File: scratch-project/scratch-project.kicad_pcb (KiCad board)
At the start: 4 copper layers, 98 x 98 mm, 13 parts, among them J1 Conn_01x10_Pin, J2 Conn_01x10_Pin, J3 Conn_02x10_Top_Bottom, J4 Conn_02x10_Top_Bottom, J5 Conn_02x10_Top_Bottom, J6 Conn_01x10_Pin

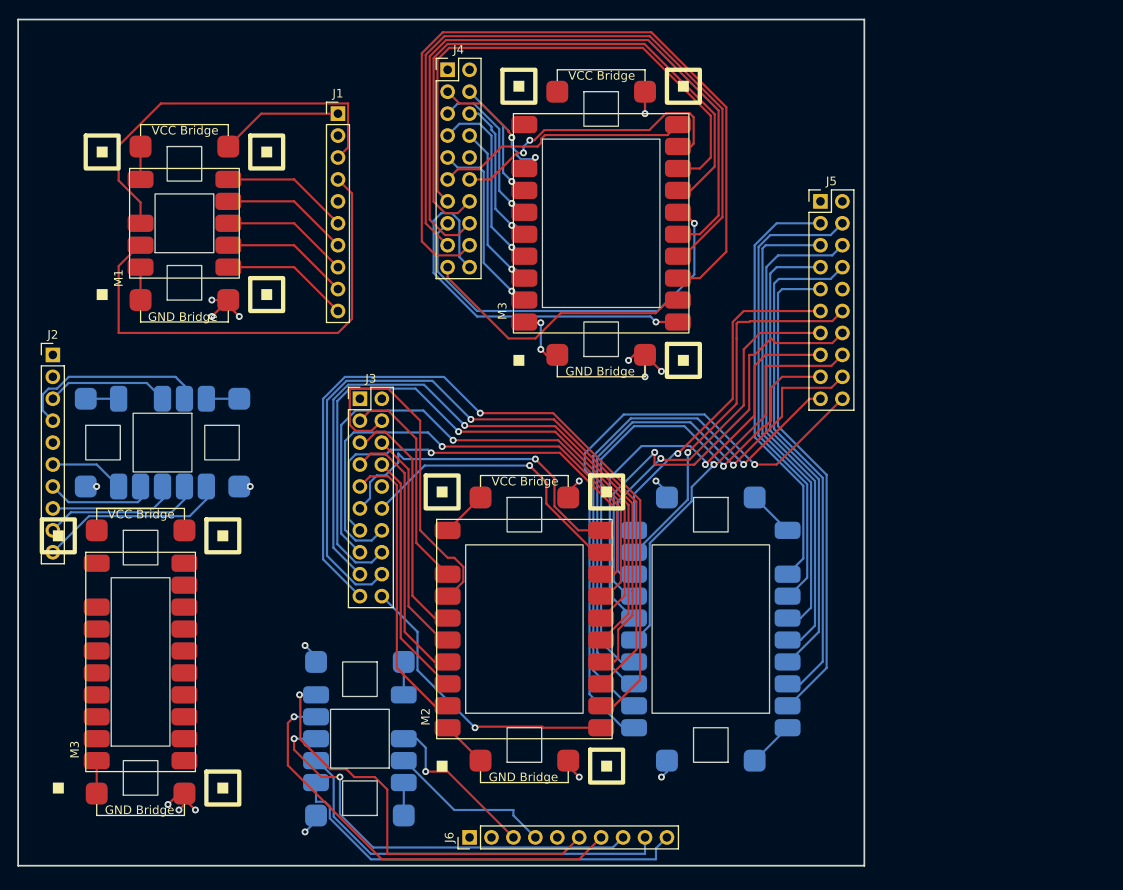
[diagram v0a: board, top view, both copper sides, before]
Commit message: fix pad sizes and schematic errors
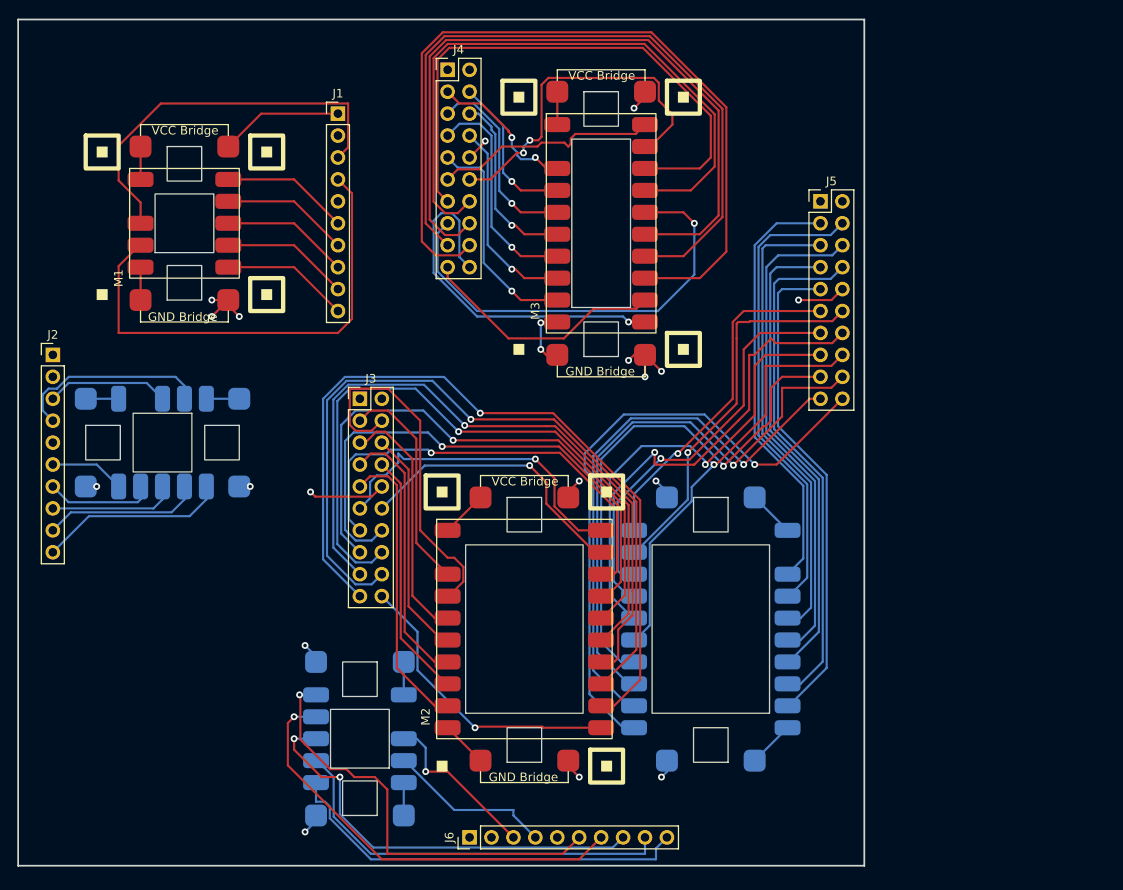
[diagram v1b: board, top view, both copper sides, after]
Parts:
- removed the M3 at (33.0, 91.4)
- M3: footprint MegaCastle:MegaCastle2x10Wide -> MegaCastle:MegaCastle2x10
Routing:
- net GND: track 24.0 -> 41.2 mm, vias 10 -> 13
- net unconnected-(M3-Board_GND-PadB2): track 7.03 -> 0.00 mm, vias 3 -> 0
- net Net-(J4-Pin_12): track 34.8 -> 40.7 mm
- net Net-(J4-Pin_16): track 80.2 -> 84.0 mm
- net Net-(J4-Pin_14): track 70.0 -> 73.8 mm
- net Net-(J4-Pin_19): track 32.6 -> 28.8 mm
- net Net-(M3-Module_VCC): track 0.00 -> 3.81 mm
- net Net-(J4-Pin_9): track 21.9 -> 25.7 mm
- net Net-(J4-Pin_8): track 19.4 -> 23.2 mm
- net Net-(J4-Pin_7): track 22.0 -> 25.8 mm
- net Net-(J4-Pin_6): track 17.4 -> 21.3 mm
- net Net-(J4-Pin_5): track 18.8 -> 22.6 mm
- net Net-(J4-Pin_20): track 46.3 -> 42.5 mm
- net Net-(J4-Pin_18): track 91.9 -> 95.8 mm
- net Net-(J4-Pin_17): track 81.4 -> 85.2 mm
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
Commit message: fix 2x10 wide footprint. add modules to scratch board
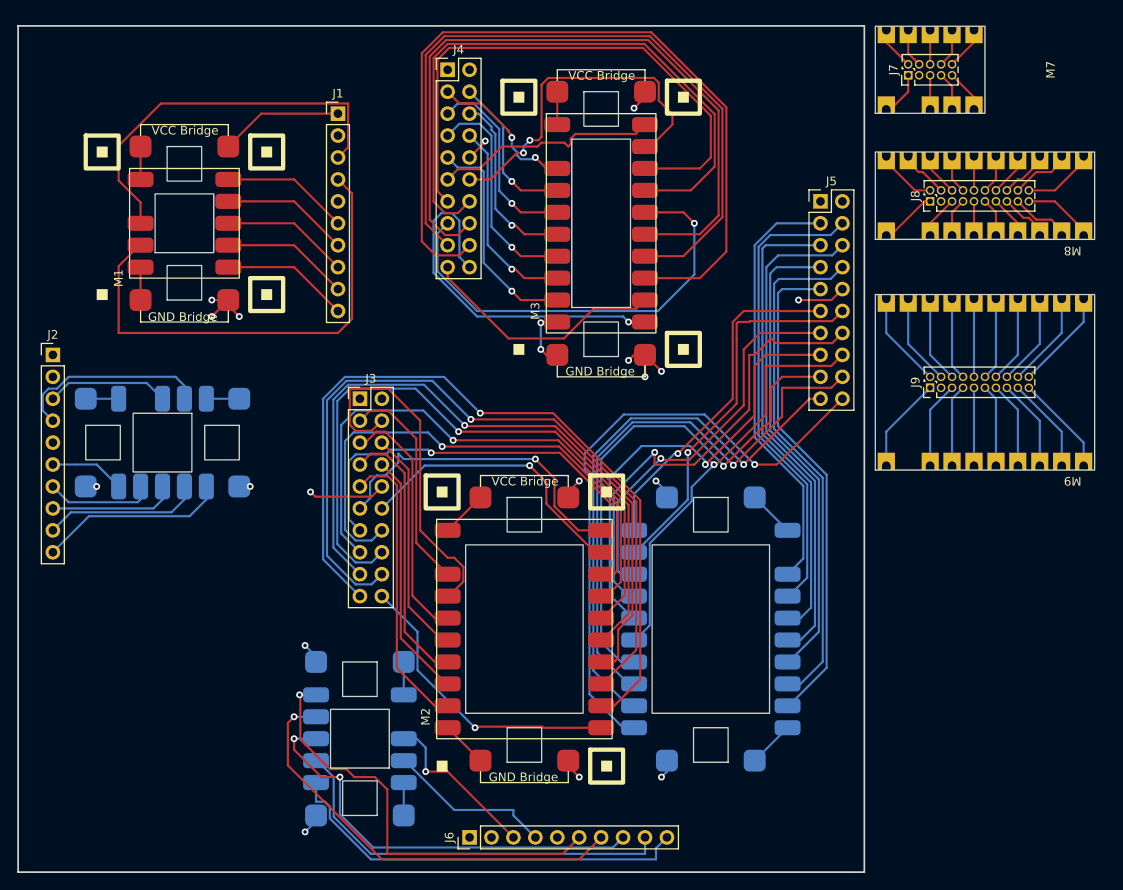
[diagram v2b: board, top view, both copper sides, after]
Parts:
- added J7: Conn_02x05_Top_Bottom, Connector_PinHeader_1.27mm:PinHeader_2x05_P1.27mm_Vertical, F.Cu at (121.9, 23.5)
- added J8: Conn_02x10_Top_Bottom, Connector_PinHeader_1.27mm:PinHeader_2x10_P1.27mm_Vertical, F.Cu at (124.5, 38.1)
- added J9: Conn_02x10_Top_Bottom, Connector_PinHeader_1.27mm:PinHeader_2x10_P1.27mm_Vertical, F.Cu at (124.5, 59.7)
- added M7: ~, MegaCastle:MegaCastle2x5-Module, F.Cu at (124.5, 22.9)
- added M8: ~, MegaCastle:MegaCastle2x10-Module, F.Cu at (130.8, 37.5)
- added M9: ~, MegaCastle:MegaCastle2x10Wide-Module, F.Cu at (130.8, 59.1)
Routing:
- net Net-(J9-Pin_10): track 0.00 -> 12.2 mm
- net Net-(J9-Pin_20): track 0.00 -> 12.2 mm
- net Net-(J9-Pin_1): track 0.00 -> 11.6 mm
- net Net-(J9-Pin_11): track 0.00 -> 11.6 mm
- net Net-(J9-Pin_9): track 0.00 -> 11.6 mm
- net Net-(J9-Pin_19): track 0.00 -> 11.6 mm
- net Net-(J9-Pin_8): track 0.00 -> 11.1 mm
- net Net-(J9-Pin_18): track 0.00 -> 11.1 mm
- net Net-(J9-Pin_12): track 0.00 -> 11.1 mm
- net Net-(J9-Pin_3): track 0.00 -> 10.6 mm
- net Net-(J9-Pin_13): track 0.00 -> 10.6 mm
- net Net-(J9-Pin_7): track 0.00 -> 10.6 mm
- net Net-(J9-Pin_17): track 0.00 -> 10.6 mm
- net Net-(J9-Pin_6): track 0.00 -> 10.1 mm
- net Net-(J9-Pin_4): track 0.00 -> 10.1 mm
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
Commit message: finish adding dummy modules to scratch board
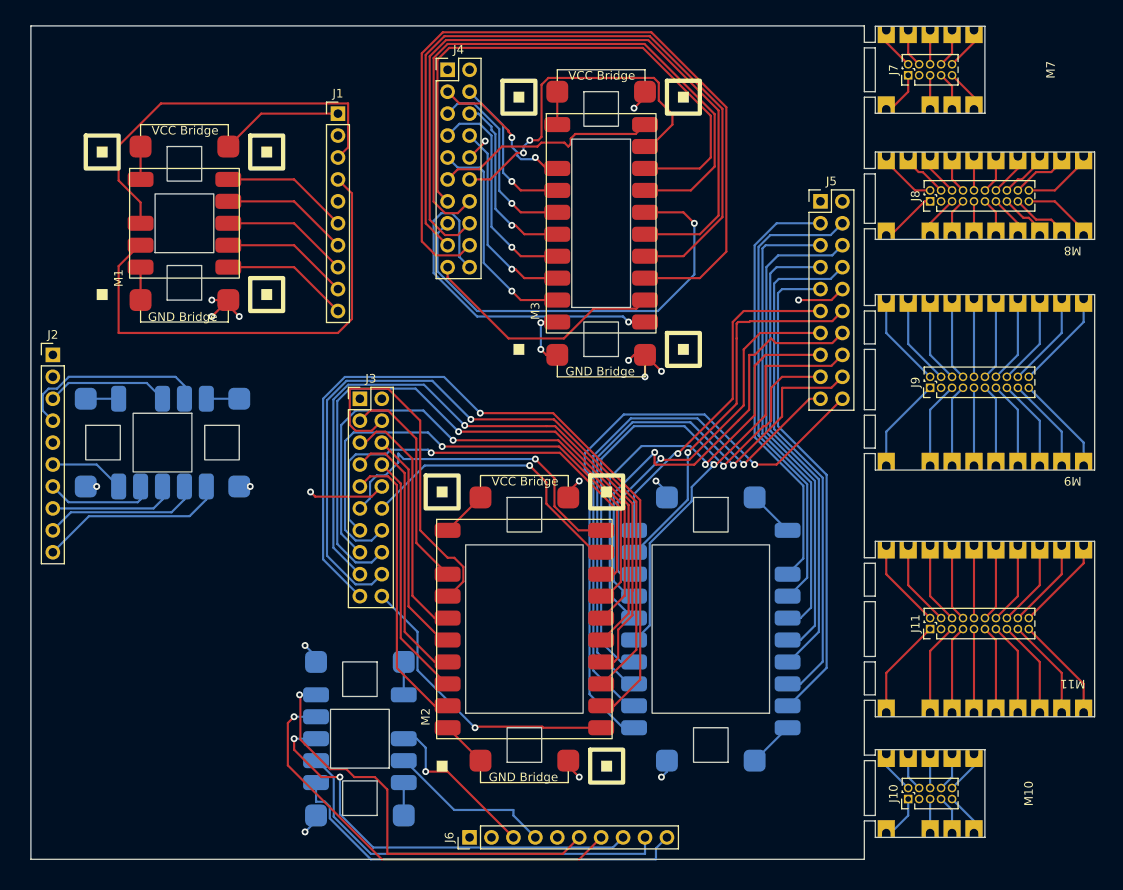
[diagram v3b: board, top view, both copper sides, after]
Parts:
- added J10: Conn_02x05_Top_Bottom, Connector_PinHeader_1.27mm:PinHeader_2x05_P1.27mm_Vertical, F.Cu at (121.9, 107.3)
- added J11: Conn_02x10_Top_Bottom, Connector_PinHeader_1.27mm:PinHeader_2x10_P1.27mm_Vertical, F.Cu at (124.5, 87.6)
- added M10: ~, MegaCastle:MegaCastle2x5-Module, F.Cu at (124.5, 106.7)
- added M11: ~, MegaCastle:MegaCastle2x10Wide-Module, F.Cu at (130.8, 87.6)
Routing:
- net Net-(J11-Pin_10): track 0.00 -> 12.8 mm
- net Net-(J11-Pin_1): track 0.00 -> 12.3 mm
- net Net-(J11-Pin_9): track 0.00 -> 12.3 mm
- net Net-(J11-Pin_8): track 0.00 -> 11.7 mm
- net Net-(J11-Pin_20): track 0.00 -> 11.5 mm
- net Net-(J11-Pin_3): track 0.00 -> 11.2 mm
- net Net-(J11-Pin_7): track 0.00 -> 11.2 mm
- net Net-(J11-Pin_11): track 0.00 -> 11.0 mm
- net Net-(J11-Pin_19): track 0.00 -> 11.0 mm
- net Net-(J11-Pin_6): track 0.00 -> 10.7 mm
- net Net-(J11-Pin_4): track 0.00 -> 10.7 mm
- net Net-(J11-Pin_18): track 0.00 -> 10.5 mm
- net Net-(J11-Pin_12): track 0.00 -> 10.5 mm
- net Net-(J11-Pin_5): track 0.00 -> 10.2 mm
- net Net-(J11-Pin_13): track 0.00 -> 9.94 mm
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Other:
- board size 98 x 98 mm -> 123.2 x 96.5 mm

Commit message: apply pcbway advice for panels
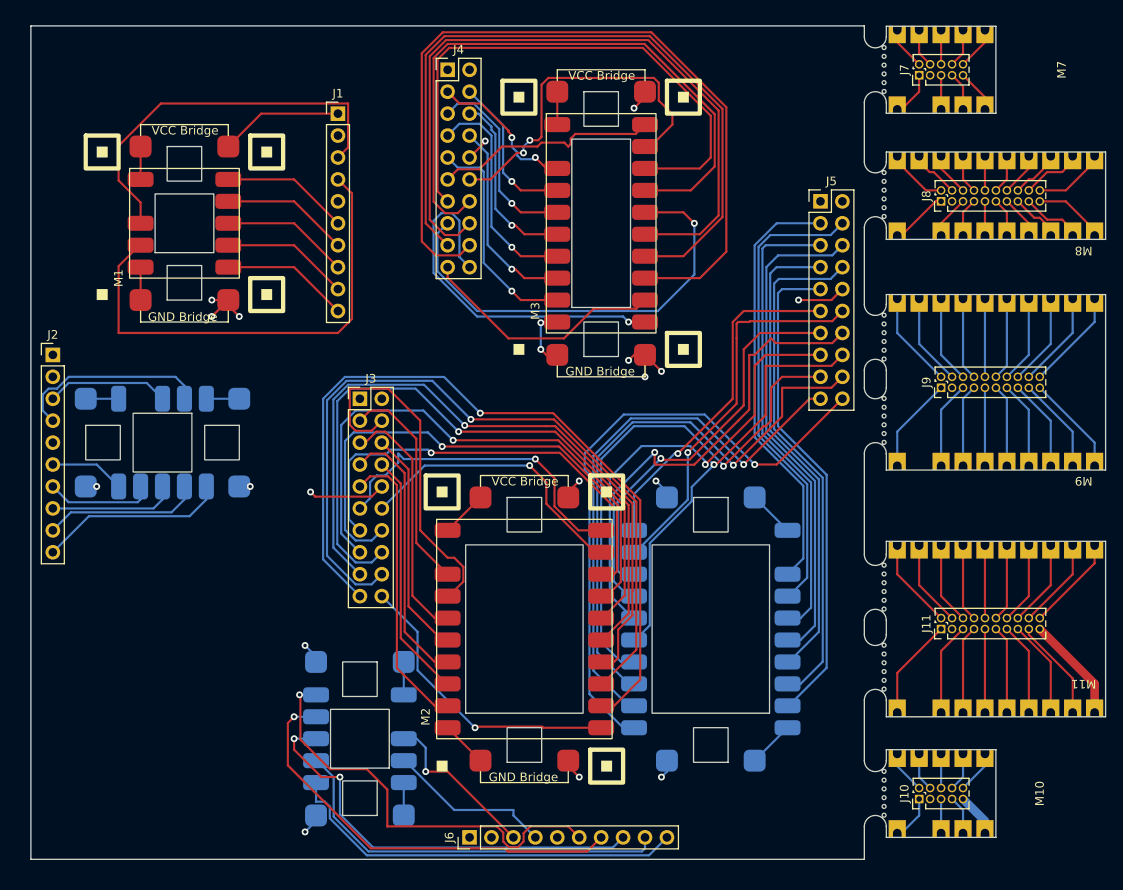
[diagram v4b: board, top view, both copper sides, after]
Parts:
- moved J11 1.27 mm to (125.7, 87.6)
- moved J8 1.27 mm to (125.7, 38.1)
- moved J9 1.27 mm to (125.7, 59.7)
- moved M10 1.27 mm to (125.7, 106.7)
- moved M11 1.27 mm to (132.1, 87.6)
- moved M7 1.27 mm to (125.7, 22.9)
- moved M8 1.27 mm to (132.1, 37.5)
- moved M9 1.27 mm to (132.1, 59.1)
- moved J10 1.27 mm to (123.2, 107.3)
- moved J7 1.27 mm to (123.2, 23.5)
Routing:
- net Net-(J6-Pin_10): track 48.2 -> 47.1 mm
- net Net-(J6-Pin_7): track 50.3 -> 49.6 mm
- net Net-(J6-Pin_9): track 47.2 -> 46.6 mm
- added copper zone on In2.Cu, net Net-(J10-Pin_1)
- added copper zone on In1.Cu, net Net-(J10-Pin_5)
- added copper zone on In2.Cu, net Net-(J11-Pin_1)
- added copper zone on In1.Cu, net Net-(J11-Pin_10)
- added copper zone on In2.Cu, net Net-(J7-Pin_1)
- added copper zone on In2.Cu, net Net-(J8-Pin_1)
- added copper zone on In1.Cu, net Net-(J8-Pin_10)
- added copper zone on In2.Cu, net Net-(J9-Pin_1)
- added copper zone on In1.Cu, net Net-(J9-Pin_10)
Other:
- board size 123.2 x 96.5 mm -> 124.5 x 96.5 mm

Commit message: update scratch project to have current module footprints
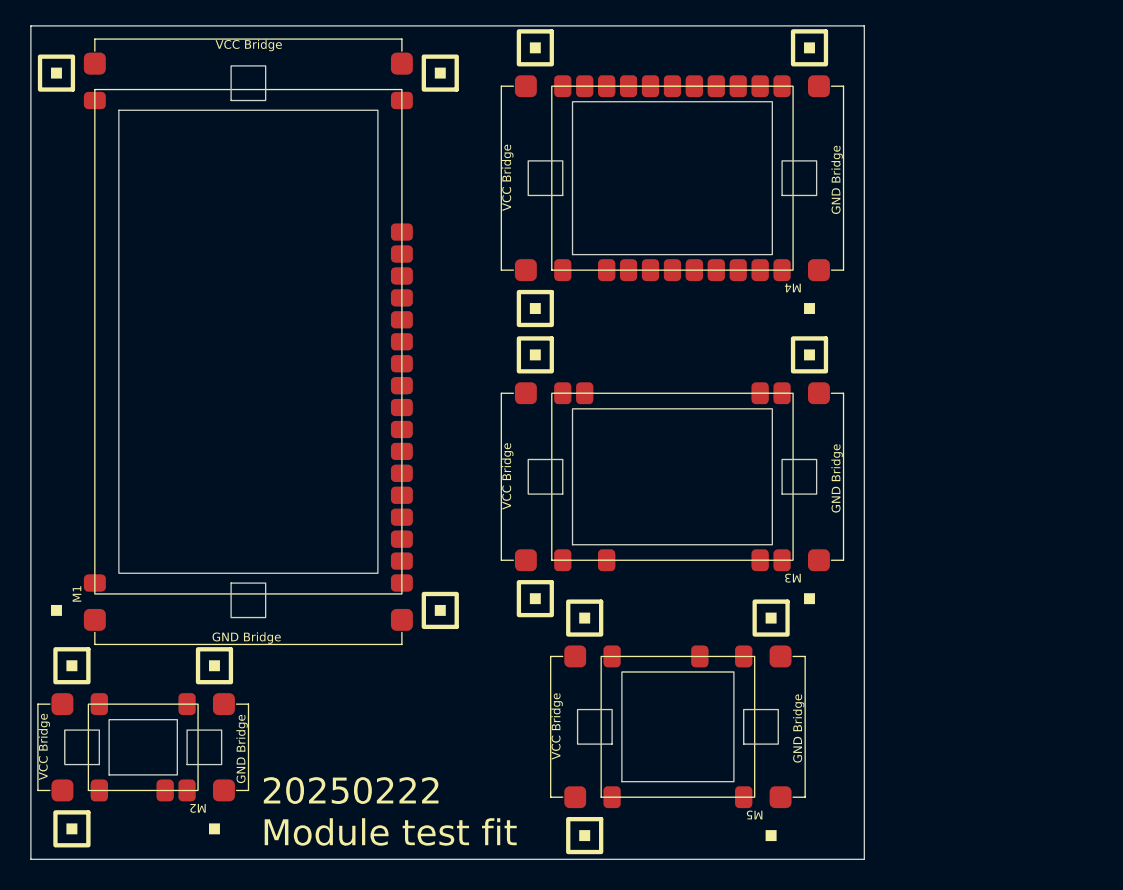
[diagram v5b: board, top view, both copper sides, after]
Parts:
- removed J1, J2, J6: Conn_01x10_Pin, Connector_PinHeader_2.54mm:PinHeader_1x10_P2.54mm_Vertical
- removed J10, J7: Conn_02x05_Top_Bottom, Connector_PinHeader_1.27mm:PinHeader_2x05_P1.27mm_Vertical
- removed J11, J8, J9: Conn_02x10_Top_Bottom, Connector_PinHeader_1.27mm:PinHeader_2x10_P1.27mm_Vertical
- removed J3, J4, J5: Conn_02x10_Top_Bottom, Connector_PinHeader_2.54mm:PinHeader_2x10_P2.54mm_Vertical
- removed M10, M7: ~, MegaCastle:MegaCastle2x5-Module
- removed M11, M9: ~, MegaCastle:MegaCastle2x10Wide-Module
- removed M6: ~, MegaCastle:MegaCastle2x5
- removed M8: ~, MegaCastle:MegaCastle2x10-Module
- M1: footprint MegaCastle:MegaCastle2x5 -> MegaCastle:MegaCastle2x23-I30.0x53.6-M80000307FFFC
- M2: footprint MegaCastle:MegaCastle2x10Wide -> MegaCastle:MegaCastle2x5-I6.4x7.9-M9C4
- M3: footprint MegaCastle:MegaCastle2x10 -> MegaCastle:MegaCastle2x11-I15.7x23.1-MA0780C
- M4: footprint MegaCastle:MegaCastle2x5 -> MegaCastle:MegaCastle2x11-I17.7x23.1-MBFFFFC; moved to F.Cu
- M5: footprint MegaCastle:MegaCastle2x10Wide -> MegaCastle:MegaCastle2x7-I12.7x13.0-M8314; moved to F.Cu
- moved M4 66.5 mm to (94.6, 35.4), turned to 90 degrees
- moved M2 46.2 mm to (33.3, 101.3), turned to 90 degrees
- moved M3 30.5 mm to (94.6, 70.0), turned to 90 degrees
- moved M1 15.6 mm to (45.5, 54.4)
- moved M5 11.9 mm to (95.2, 99.0), turned to 90 degrees
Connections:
- M1 pad 1: Net-(M1-Module_VCC) -> unconnected-(M1-VCC-Pad1)
- M1 pad A1: Net-(M1-Module_VCC) -> unconnected-(M1-Module_VCC-PadA1)
- M1 pad A2: VCC -> unconnected-(M1-Board_VCC-PadA2)
- M1 pad B1: Net-(M1-GND) -> unconnected-(M1-Module_GND-PadB1)
- M1 pad B2: GND -> unconnected-(M1-Board_GND-PadB2)
- M2 pad 1: Net-(M2-Module_VCC) -> unconnected-(M2-VCC-Pad1)
- M2 pad 10: Net-(M2-GND) -> unconnected-(M2-Pad10)
- M2 pad 4: Net-(J3-Pin_4) -> unconnected-(M2-Pad4)
- M2 pad 5: Net-(J3-Pin_5) -> unconnected-(M2-GND-Pad5)
- M2 pad 6: Net-(J3-Pin_6) -> unconnected-(M2-Pad6)
- M2 pad A1: Net-(M2-Module_VCC) -> unconnected-(M2-Module_VCC-PadA1)
- M2 pad A2: VCC -> unconnected-(M2-Board_VCC-PadA2)
- M2 pad B1: Net-(M2-GND) -> unconnected-(M2-Module_GND-PadB1)
- M2 pad B2: GND -> unconnected-(M2-Board_GND-PadB2)
- M3 pad 1: Net-(M3-Module_VCC) -> unconnected-(M3-VCC-Pad1)
- M3 pad 10: Net-(M3-GND) -> unconnected-(M3-Pad10)
- M3 pad 11: Net-(J4-Pin_11) -> unconnected-(M3-GND-Pad11)
- M3 pad 12: Net-(J4-Pin_12) -> unconnected-(M3-Pad12)
- M3 pad 13: Net-(J4-Pin_13) -> unconnected-(M3-Pad13)
- M3 pad 3: Net-(J4-Pin_3) -> unconnected-(M3-Pad3)
- M3 pad A1: Net-(M3-Module_VCC) -> unconnected-(M3-Module_VCC-PadA1)
- M3 pad A2: VCC -> unconnected-(M3-Board_VCC-PadA2)
- M3 pad B1: Net-(M3-GND) -> unconnected-(M3-Module_GND-PadB1)
- M3 pad B2: GND -> unconnected-(M3-Board_GND-PadB2)
- M4 pad 1: Net-(M4-Module_VCC) -> unconnected-(M4-VCC-Pad1)
- M4 pad 10: Net-(J2-Pin_10) -> unconnected-(M4-Pad10)
- M4 pad 3: Net-(J2-Pin_3) -> unconnected-(M4-Pad3)
- M4 pad 4: Net-(J2-Pin_4) -> unconnected-(M4-Pad4)
- M4 pad 5: Net-(M4-GND) -> unconnected-(M4-Pad5)
- M4 pad 6: Net-(J2-Pin_6) -> unconnected-(M4-Pad6)
- M4 pad 7: Net-(J2-Pin_7) -> unconnected-(M4-Pad7)
- M4 pad 8: Net-(J2-Pin_8) -> unconnected-(M4-Pad8)
- M4 pad 9: Net-(J2-Pin_9) -> unconnected-(M4-Pad9)
- M4 pad A1: Net-(M4-Module_VCC) -> unconnected-(M4-Module_VCC-PadA1)
- M4 pad A2: VCC -> unconnected-(M4-Board_VCC-PadA2)
- M4 pad B1: Net-(M4-GND) -> unconnected-(M4-Module_GND-PadB1)
- M4 pad B2: GND -> unconnected-(M4-Board_GND-PadB2)
- M5 pad 1: Net-(M5-Module_VCC) -> unconnected-(M5-VCC-Pad1)
- M5 pad 12: Net-(J5-Pin_12) -> unconnected-(M5-Pad12)
- M5 pad 14: Net-(J5-Pin_14) -> unconnected-(M5-Pad14)
- M5 pad 7: Net-(J5-Pin_7) -> unconnected-(M5-GND-Pad7)
- M5 pad 8: Net-(J5-Pin_8) -> unconnected-(M5-Pad8)
- M5 pad A1: Net-(M5-Module_VCC) -> unconnected-(M5-Module_VCC-PadA1)
- M5 pad A2: VCC -> unconnected-(M5-Board_VCC-PadA2)
- M5 pad B1: Net-(M5-GND) -> unconnected-(M5-Module_GND-PadB1)
- M5 pad B2: GND -> unconnected-(M5-Board_GND-PadB2)
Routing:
- net Net-(J4-Pin_18): track 95.8 -> 0.00 mm
- net Net-(J3-Pin_19): track 94.9 -> 0.00 mm, vias 1 -> 0
- net Net-(J3-Pin_18): track 91.6 -> 0.00 mm, vias 1 -> 0
- net Net-(J4-Pin_17): track 85.2 -> 0.00 mm
- net Net-(J4-Pin_16): track 84.0 -> 0.00 mm
- net Net-(J3-Pin_17): track 83.3 -> 0.00 mm, vias 1 -> 0
- net Net-(J3-Pin_16): track 80.0 -> 0.00 mm, vias 1 -> 0
- net Net-(J4-Pin_14): track 73.8 -> 0.00 mm
- net Net-(J5-Pin_20): track 72.1 -> 0.00 mm, vias 1 -> 0
- net Net-(J3-Pin_15): track 67.9 -> 0.00 mm, vias 1 -> 0
- net Net-(J5-Pin_18): track 66.7 -> 0.00 mm, vias 1 -> 0
- net Net-(J4-Pin_13): track 65.4 -> 0.00 mm
- net Net-(J5-Pin_19): track 64.7 -> 0.00 mm, vias 1 -> 0
- net Net-(J3-Pin_14): track 63.0 -> 0.00 mm, vias 1 -> 0
- net Net-(J5-Pin_17): track 61.4 -> 0.00 mm, vias 1 -> 0
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- removed copper zone on In1.Cu, net GND
- removed copper zone on In2.Cu, net Net-(J10-Pin_1)
- removed copper zone on In1.Cu, net Net-(J10-Pin_5)
- removed copper zone on In2.Cu, net Net-(J11-Pin_1)
- removed copper zone on In1.Cu, net Net-(J11-Pin_10)
- removed copper zone on In2.Cu, net Net-(J7-Pin_1)
- removed copper zone on In2.Cu, net Net-(J8-Pin_1)
- removed copper zone on In1.Cu, net Net-(J8-Pin_10)
- removed copper zone on In2.Cu, net Net-(J9-Pin_1)
- removed copper zone on In1.Cu, net Net-(J9-Pin_10)
- removed copper zone on In2.Cu, net VCC
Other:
- board size 124.5 x 96.5 mm -> 96.5 x 96.5 mm
- copper layers 4 -> 2
- board text added: "20250222 Module test fit"
